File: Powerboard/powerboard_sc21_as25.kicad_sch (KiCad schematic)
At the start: 43 parts

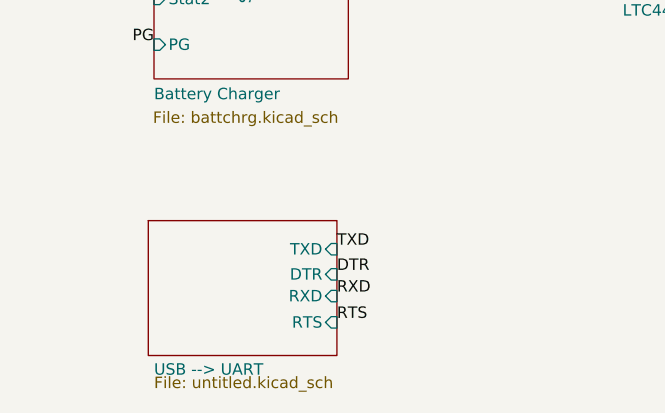
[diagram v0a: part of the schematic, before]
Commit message: added vbus to 3.3v converter
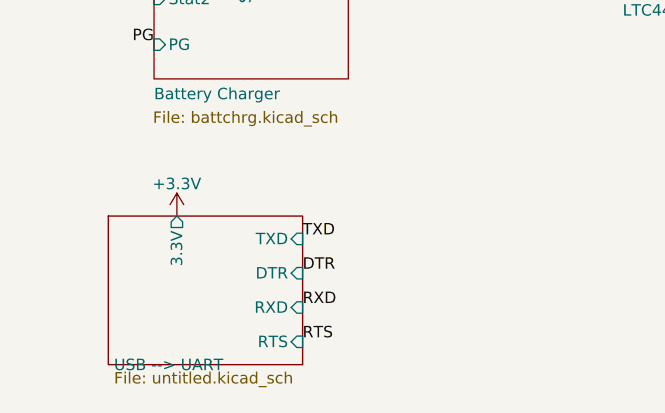
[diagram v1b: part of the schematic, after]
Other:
- sheet USB --> UART ports: added 3.3V; removed none
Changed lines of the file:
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@@
     (effects (font (size 1.27 1.27)) (justify right bottom))
   )
-  (label "DTR" (at 67.31 174.117 0)
+  (label "DTR" (at 63.5 173.99 0)
     (effects (font (size 1.27 1.27)) (justify left bottom))
   )
@@
     (effects (font (size 1.27 1.27)) (justify left bottom))
   )
-  (label "TXD" (at 67.31 171.323 0)
+  (label "TXD" (at 63.5 170.18 0)
     (effects (font (size 1.27 1.27)) (justify left bottom))
   )
@@
     (effects (font (size 1.27 1.27)) (justify left bottom))
   )
-  (label "RXD" (at 67.31 176.53 0)
+  (label "RXD" (at 63.5 177.8 0)
     (effects (font (size 1.27 1.27)) (justify left bottom))
   )
@@
     (effects (font (size 1.27 1.27)) (justify left bottom))
   )
-  (label "RTS" (at 67.31 179.451 0)
+  (label "RTS" (at 63.5 181.61 0)
     (effects (font (size 1.27 1.27)) (justify left bottom))
   )
@@
     (pin "1")
   )
+  (symbol (lib_id "power:+3.3V") (at 49.53 167.64 0) (unit 1)
+    (in_bom yes) (on_board yes) (fields_autoplaced)
+    (property "Reference" "#PWR?" (id 0) (at 49.53 171.45 0)
+      (effects (font (size 1.27 1.27)) hide)
+    )
+    (property "Value" "+3.3V" (id 1) (at 49.53 164.0642 0))
+    (property "Footprint" "" (id 2) (at 49.53 167.64 0)
+      (effects (font (size 1.27 1.27)) hide)
+    )
+    (property "Datasheet" "" (id 3) (at 49.53 167.64 0)
+      (effects (font (size 1.27 1.27)) hide)
+    )
+    (pin "1")
+  )
   (symbol (lib_id "power:GND") (at 34.29 34.29 0) (unit 1)
     (in_bom yes) (on_board yes)
@@
     )
   )
-  (sheet (at 46.355 168.148) (size 20.955 14.986)
+  (sheet (at 41.91 167.64) (size 21.59 16.51)
     (stroke (width 0.1524) (type solid) (color 0 0 0 0))
     (fill (color 0 0 0 0.0000))
-    (property "Sheet name" "USB --> UART" (id 0) (at 46.99 185.42 0)
+    (property "Sheet name" "USB --> UART" (id 0) (at 42.545 184.912 0)
       (effects (font (size 1.27 1.27)) (justify left bottom))
     )
-    (property "Sheet file" "untitled.kicad_sch" (id 1) (at 46.99 185.42 0)
+    (property "Sheet file" "untitled.kicad_sch" (id 1) (at 42.545 184.912 0)
       (effects (font (size 1.27 1.27)) (justify left top))
     )
-    (pin "RXD" input (at 67.31 176.53 0)
+    (pin "DTR" input (at 63.5 173.99 0)
       (effects (font (size 1.27 1.27)) (justify right))
     )
-    (pin "DTR" input (at 67.31 174.117 0)
+    (pin "RXD" input (at 63.5 177.8 0)
       (effects (font (size 1.27 1.27)) (justify right))
     )
-    (pin "TXD" input (at 67.31 171.323 0)
+    (pin "TXD" input (at 63.5 170.18 0)
       (effects (font (size 1.27 1.27)) (justify right))
     )
-    (pin "RTS" input (at 67.31 179.451 0)
+    (pin "RTS" input (at 63.5 181.61 0)
+      (effects (font (size 1.27 1.27)) (justify right))
+    )
+    (pin "3.3V" output (at 49.53 167.64 90)
       (effects (font (size 1.27 1.27)) (justify right))
     )
@@
       (reference "#PWR?") (unit 1) (value "GND") (footprint "")
     )
+    (path "/b1853ee1-af2e-49ab-93e4-e29b2d9f793d/01b8be9d-07b4-4ed5-be0d-c2f1fdf5d66a"
+      (reference "#PWR?") (unit 1) (value "GND") (footprint "")
+    )
+    (path "/b1853ee1-af2e-49ab-93e4-e29b2d9f793d/0b35d416-2ef3-43da-b21e-3b5705733789"
+      (reference "#PWR?") (unit 1) (value "GND") (footprint "")
+    )
     (path "/1669a8b1-50be-401b-a425-d2de253f88c4"
       (reference "#PWR?") (unit 1) (value "GND") (footprint "")
@@
       (reference "#PWR?") (unit 1) (value "GND") (footprint "")
     )
+    (path "/b1853ee1-af2e-49ab-93e4-e29b2d9f793d/3e7fe04a-5983-45ca-b62b-77d9b2d44905"
+      (reference "#PWR?") (unit 1) (value "VBUS") (footprint "")
+    )
+    (path "/b1853ee1-af2e-49ab-93e4-e29b2d9f793d/53c2082f-14d4-4f8b-b15e-479d0706e172"
+      (reference "#PWR?") (unit 1) (value "GND") (footprint "")
+    )
     (path "/b1853ee1-af2e-49ab-93e4-e29b2d9f793d/5b143561-1a97-4458-adc9-ad22ebe9d9fc"
       (reference "#PWR?") (unit 1) (value "GND") (footprint "")
@@
       (reference "#PWR?") (unit 1) (value "+3.3V") (footprint "")
     )
+    (path "/7cdd1385-4bcf-4b79-addf-8e4216a2d506"
+      (reference "#PWR?") (unit 1) (value "+3.3V") (footprint "")
+    )
+    (path "/b1853ee1-af2e-49ab-93e4-e29b2d9f793d/7d0aa032-9b1f-469d-85cd-a28c4fe41bd4"
+      (reference "#PWR?") (unit 1) (value "GND") (footprint "")
+    )
     (path "/00000000-0000-0000-0000-000061beb629/7d5bd6a8-4feb-43d7-80fd-001ff51c8cd3"
       (reference "#PWR?") (unit 1) (value "GND") (footprint "")
@@
       (reference "#PWR?") (unit 1) (value "GND") (footprint "")
     )
+    (path "/b1853ee1-af2e-49ab-93e4-e29b2d9f793d/a2635da5-8463-46db-9199-0a173306f41b"
+      (reference "#PWR?") (unit 1) (value "GND") (footprint "")
+    )
     (path "/a313493b-a610-47cf-bd19-ffd9120f658d"
       (reference "#PWR?") (unit 1) (value "+3.3V") (footprint "")
     )
+    (path "/b1853ee1-af2e-49ab-93e4-e29b2d9f793d/a4e693f1-e8be-4638-b20a-f43f39a9ed46"
+      (reference "#PWR?") (unit 1) (value "GND") (footprint "")
+    )
+    (path "/b1853ee1-af2e-49ab-93e4-e29b2d9f793d/b36e399c-fd07-48dc-9ff5-2204b47fbf43"
+      (reference "#PWR?") (unit 1) (value "GND") (footprint "")
+    )
     (path "/b1853ee1-af2e-49ab-93e4-e29b2d9f793d/b3eace1a-8e3b-4ab2-9e5a-cfb096644465"
       (reference "#PWR?") (unit 1) (value "+3.3V") (footprint "")
     )
+    (path "/b1853ee1-af2e-49ab-93e4-e29b2d9f793d/ba910aa5-1c14-49e2-8e02-8063979f6496"
+      (reference "#PWR?") (unit 1) (value "GND") (footprint "")
+    )
     (path "/c564c3d3-cbea-454d-bfac-67a8a729bdf8"
       (reference "#PWR?") (unit 1) (value "GND") (footprint "")
@@
       (reference "C?") (unit 1) (value "CP") (footprint "")
     )
+    (path "/b1853ee1-af2e-49ab-93e4-e29b2d9f793d/02e53112-42dc-4e92-9413-ebf4a1fcdc4a"
+      (reference "C?") (unit 1) (value "10uF") (footprint "Capacitor_SMD:C_0603_1608Metric")
+    )
+    (path "/b1853ee1-af2e-49ab-93e4-e29b2d9f793d/19b6fdb7-c2da-4e40-b2bb-be0a937611f0"
+      (reference "C?") (unit 1) (value "4.7uF") (footprint "Capacitor_SMD:C_0603_1608Metric")
+    )
+    (path "/b1853ee1-af2e-49ab-93e4-e29b2d9f793d/1fd2c422-69ae-40c0-b3b2-cb505077339f"
+      (reference "C?") (unit 1) (value "0.1uF") (footprint "Capacitor_SMD:C_0603_1608Metric")
+    )
     (path "/b1853ee1-af2e-49ab-93e4-e29b2d9f793d/23d7c986-ca1f-4e54-a551-aae82e6382e3"
       (reference "C?") (unit 1) (value "1.0muF") (footprint "")
@@
       (reference "C?") (unit 1) (value "1μF") (footprint "")
     )
+    (path "/b1853ee1-af2e-49ab-93e4-e29b2d9f793d/3bf9d9e3-3041-4ea1-ad6f-34bc1dc2c61a"
+      (reference "C?") (unit 1) (value "1uF") (footprint "Capacitor_SMD:C_0603_1608Metric")
+    )
     (path "/b1853ee1-af2e-49ab-93e4-e29b2d9f793d/400c7a12-6a3b-4007-bebb-25fa9d8ef61f"
       (reference "C?") (unit 1) (value "0.1muF") (footprint "")
@@
       (reference "C?") (unit 1) (value "4.7muF") (footprint "")
     )
+    (path "/b1853ee1-af2e-49ab-93e4-e29b2d9f793d/900cbe97-baf8-4c02-a824-562c02dac994"
+      (reference "C?") (unit 1) (value "10uF") (footprint "Capacitor_SMD:C_0603_1608Metric")
+    )
     (path "/96d17e45-ecc3-4647-9d46-ac8a08d006bc"
       (reference "C?") (unit 1) (value "1.5pF") (footprint "")
@@
       (reference "R?") (unit 1) (value "470Ω") (footprint "")
     )
+    (path "/b1853ee1-af2e-49ab-93e4-e29b2d9f793d/08599c5d-18df-4076-8d95-9afe2b0b7202"
+      (reference "R?") (unit 1) (value "100k") (footprint "Resistor_SMD:R_0603_1608Metric")
+    )
+    (path "/b1853ee1-af2e-49ab-93e4-e29b2d9f793d/1f07eb91-ef46-4237-a9f5-5823737e0d44"
+      (reference "R?") (unit 1) (value "47k") (footprint "Resistor_SMD:R_0603_1608Metric")
+    )
     (path "/b1853ee1-af2e-49ab-93e4-e29b2d9f793d/3fdc1205-170d-4bad-a583-c2274b810ac0"
       (reference "R?") (unit 1) (value "47k") (footprint "")
@@
       (reference "R?") (unit 1) (value "10kΩ") (footprint "")
     )
+    (path "/b1853ee1-af2e-49ab-93e4-e29b2d9f793d/a6bf9111-8852-4077-bff6-579c92450f65"
+      (reference "R?") (unit 1) (value "147k") (footprint "Resistor_SMD:R_0603_1608Metric")
+    )
     (path "/b1853ee1-af2e-49ab-93e4-e29b2d9f793d/a97adbbf-7a4b-4c74-8340-d0fb219e42dc"
       (reference "R?") (unit 1) (value "5.1k") (footprint "")
@@
       (reference "U?") (unit 1) (value "LTC4412xS6") (footprint "Package_TO_SOT_SMD:TSOT-23-6")
     )
-  )
+    (path "/b1853ee1-af2e-49ab-93e4-e29b2d9f793d/1444d49f-1253-44c6-b265-5d56e5057df7"
+      (reference "U?") (unit 1) (value "RT9025-25GSP") (footprint "Package_SO:SOP-8_3.9x4.9mm_P1.27mm")
+    )
+    (path "/b1853ee1-af2e-49ab-93e4-e29b2d9f793d/8f776380-fcbf-4da6-96c0-055517925d40"
+      (reference "U?") (unit 1) (value "LTC4411") (footprint "Package_TO_SOT_SMD:SOT-23-5")
+    )
+  )

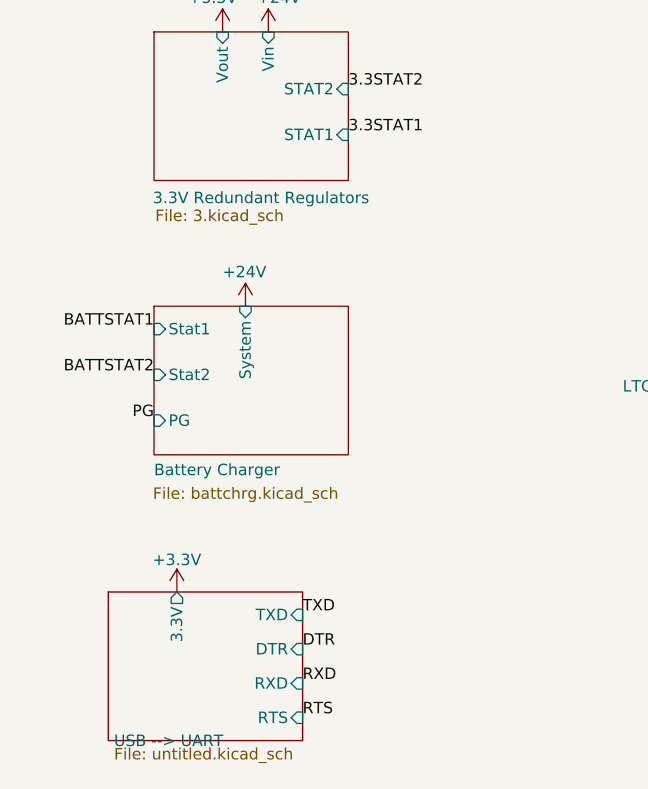
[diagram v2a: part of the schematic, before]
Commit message: Added thermistor resistor for specific thermistor
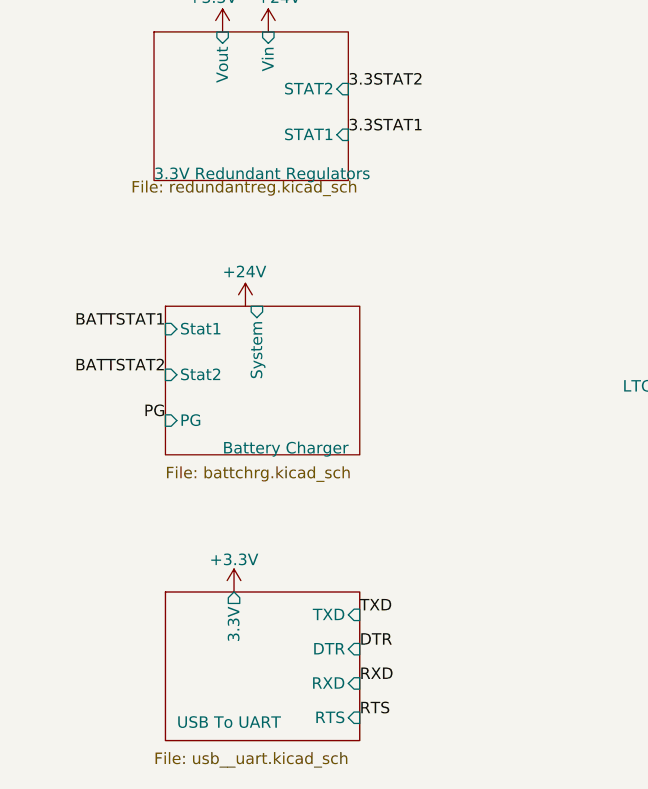
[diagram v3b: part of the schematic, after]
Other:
- sheet USB --> UART renamed USB To UART
- sheet 3.3V Redundant Regulators: file 3.kicad_sch -> redundantreg.kicad_sch
- sheet USB To UART: file untitled.kicad_sch -> usb__uart.kicad_sch
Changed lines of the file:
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@@
     (effects (font (size 1.27 1.27)) (justify left bottom))
   )
-  (label "BATTSTAT1" (at 46.99 138.43 180)
+  (label "BATTSTAT1" (at 48.26 138.43 180)
     (effects (font (size 1.27 1.27)) (justify right bottom))
   )
@@
     (effects (font (size 1.27 1.27)) (justify right bottom))
   )
-  (label "DTR" (at 63.5 173.99 0)
+  (label "DTR" (at 69.85 173.99 0)
     (effects (font (size 1.27 1.27)) (justify left bottom))
   )
@@
     (effects (font (size 1.27 1.27)) (justify left bottom))
   )
-  (label "TXD" (at 63.5 170.18 0)
+  (label "TXD" (at 69.85 170.18 0)
     (effects (font (size 1.27 1.27)) (justify left bottom))
   )
@@
     (effects (font (size 1.27 1.27)) (justify left bottom))
   )
-  (label "RXD" (at 63.5 177.8 0)
+  (label "RXD" (at 69.85 177.8 0)
     (effects (font (size 1.27 1.27)) (justify left bottom))
   )
@@
     (effects (font (size 1.27 1.27)) (justify left bottom))
   )
-  (label "RTS" (at 63.5 181.61 0)
+  (label "RTS" (at 69.85 181.61 0)
     (effects (font (size 1.27 1.27)) (justify left bottom))
   )
@@
     (effects (font (size 1.27 1.27)) (justify right bottom))
   )
-  (label "BATTSTAT2" (at 46.99 143.51 180)
+  (label "BATTSTAT2" (at 48.26 143.51 180)
     (effects (font (size 1.27 1.27)) (justify right bottom))
   )
@@
     (effects (font (size 1.27 1.27)) (justify left bottom))
   )
-  (label "PG" (at 46.99 148.59 180)
+  (label "PG" (at 48.26 148.59 180)
     (effects (font (size 1.27 1.27)) (justify right bottom))
   )
@@
     (pin "1")
   )
-  (symbol (lib_id "power:+3.3V") (at 49.53 167.64 0) (unit 1)
+  (symbol (lib_id "power:+3.3V") (at 55.88 167.64 0) (unit 1)
     (in_bom yes) (on_board yes) (fields_autoplaced)
-    (property "Reference" "#PWR?" (id 0) (at 49.53 171.45 0)
-      (effects (font (size 1.27 1.27)) hide)
-    )
-    (property "Value" "+3.3V" (id 1) (at 49.53 164.0642 0))
-    (property "Footprint" "" (id 2) (at 49.53 167.64 0)
-      (effects (font (size 1.27 1.27)) hide)
-    )
-    (property "Datasheet" "" (id 3) (at 49.53 167.64 0)
+    (property "Reference" "#PWR?" (id 0) (at 55.88 171.45 0)
+      (effects (font (size 1.27 1.27)) hide)
+    )
+    (property "Value" "+3.3V" (id 1) (at 55.88 164.0642 0))
+    (property "Footprint" "" (id 2) (at 55.88 167.64 0)
+      (effects (font (size 1.27 1.27)) hide)
+    )
+    (property "Datasheet" "" (id 3) (at 55.88 167.64 0)
       (effects (font (size 1.27 1.27)) hide)
     )
@@
     (pin "2")
   )
-  (sheet (at 46.99 135.89) (size 21.59 16.51)
+  (sheet (at 48.26 135.89) (size 21.59 16.51)
     (stroke (width 0) (type solid) (color 0 0 0 0))
     (fill (color 0 0 0 0.0000))
-    (property "Sheet name" "Battery Charger" (id 0) (at 46.99 154.813 0)
+    (property "Sheet name" "Battery Charger" (id 0) (at 54.61 152.4 0)
       (effects (font (size 1.27 1.27)) (justify left bottom))
     )
-    (property "Sheet file" "battchrg.kicad_sch" (id 1) (at 46.863 155.956 0)
+    (property "Sheet file" "battchrg.kicad_sch" (id 1) (at 48.26 153.67 0)
       (effects (font (size 1.27 1.27)) (justify left top))
     )
-    (pin "System" input (at 57.15 135.89 90)
+    (pin "System" input (at 58.42 135.89 90)
       (effects (font (size 1.27 1.27)) (justify right))
     )
-    (pin "Stat1" input (at 46.99 138.43 180)
-      (effects (font (size 1.27 1.27)) (justify left))
-    )
-    (pin "Stat2" input (at 46.99 143.51 180)
-      (effects (font (size 1.27 1.27)) (justify left))
-    )
-    (pin "PG" input (at 46.99 148.59 180)
+    (pin "Stat1" input (at 48.26 138.43 180)
+      (effects (font (size 1.27 1.27)) (justify left))
+    )
+    (pin "Stat2" input (at 48.26 143.51 180)
+      (effects (font (size 1.27 1.27)) (justify left))
+    )
+    (pin "PG" input (at 48.26 148.59 180)
       (effects (font (size 1.27 1.27)) (justify left))
     )
@@
     (stroke (width 0) (type solid) (color 0 0 0 0))
     (fill (color 0 0 0 0.0000))
-    (property "Sheet name" "3.3V Redundant Regulators" (id 0) (at 46.863 124.587 0)
+    (property "Sheet name" "3.3V Redundant Regulators" (id 0) (at 46.99 121.92 0)
       (effects (font (size 1.27 1.27)) (justify left bottom))
     )
-    (property "Sheet file" "3.kicad_sch" (id 1) (at 47.117 125.095 0)
+    (property "Sheet file" "redundantreg.kicad_sch" (id 1) (at 44.45 121.92 0)
       (effects (font (size 1.27 1.27)) (justify left top))
     )
@@
     )
   )
-  (sheet (at 41.91 167.64) (size 21.59 16.51)
+  (sheet (at 48.26 167.64) (size 21.59 16.51)
     (stroke (width 0.1524) (type solid) (color 0 0 0 0))
     (fill (color 0 0 0 0.0000))
-    (property "Sheet name" "USB --> UART" (id 0) (at 42.545 184.912 0)
+    (property "Sheet name" "USB To UART" (id 0) (at 49.53 182.88 0)
       (effects (font (size 1.27 1.27)) (justify left bottom))
     )
-    (property "Sheet file" "untitled.kicad_sch" (id 1) (at 42.545 184.912 0)
+    (property "Sheet file" "usb__uart.kicad_sch" (id 1) (at 46.99 185.42 0)
       (effects (font (size 1.27 1.27)) (justify left top))
     )
-    (pin "DTR" input (at 63.5 173.99 0)
+    (pin "DTR" input (at 69.85 173.99 0)
       (effects (font (size 1.27 1.27)) (justify right))
     )
-    (pin "RXD" input (at 63.5 177.8 0)
+    (pin "RXD" input (at 69.85 177.8 0)
       (effects (font (size 1.27 1.27)) (justify right))
     )
-    (pin "TXD" input (at 63.5 170.18 0)
+    (pin "TXD" input (at 69.85 170.18 0)
       (effects (font (size 1.27 1.27)) (justify right))
     )
-    (pin "RTS" input (at 63.5 181.61 0)
+    (pin "RTS" input (at 69.85 181.61 0)
       (effects (font (size 1.27 1.27)) (justify right))
     )
-    (pin "3.3V" output (at 49.53 167.64 90)
+    (pin "3.3V" output (at 55.88 167.64 90)
       (effects (font (size 1.27 1.27)) (justify right))
     )
@@
     )
     (path "/00000000-0000-0000-0000-000061beb629/00000000-0000-0000-0000-000061c1bdf7"
-      (reference "J1") (unit 1) (value "Thermistor Connection") (footprint "")
+      (reference "J1") (unit 1) (value "Thermistor Connection 103AT NTC") (footprint "")
     )
     (path "/00000000-0000-0000-0000-0000620cf89f"

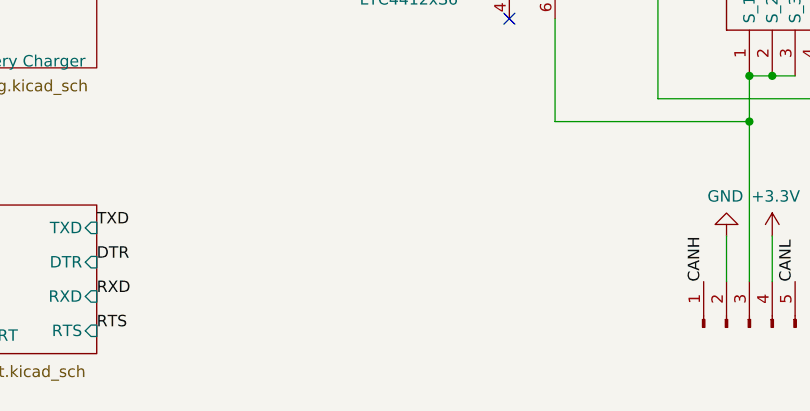
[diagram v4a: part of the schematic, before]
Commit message: removed battery monitor
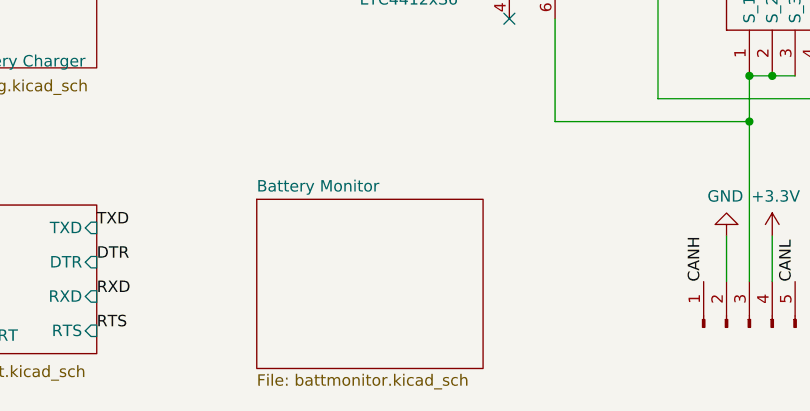
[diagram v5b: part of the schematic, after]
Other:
- added sheet Battery Monitor (battmonitor.kicad_sch)
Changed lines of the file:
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@@
+    )
+  )
+  (sheet (at 87.63 167.005) (size 25.146 18.796) (fields_autoplaced)
+    (stroke (width 0.1524) (type solid) (color 0 0 0 0))
+    (fill (color 0 0 0 0.0000))
+    (property "Sheet name" "Battery Monitor" (id 0) (at 87.63 166.2934 0)
+      (effects (font (size 1.27 1.27)) (justify left bottom))
+    )
+    (property "Sheet file" "battmonitor.kicad_sch" (id 1) (at 87.63 186.3856 0)
+      (effects (font (size 1.27 1.27)) (justify left top))
     )
   )
@@
     (path "/00000000-0000-0000-0000-000061f04c1a" (page "3"))
     (path "/b1853ee1-af2e-49ab-93e4-e29b2d9f793d" (page "4"))
+    (path "/33e9abb9-e634-4336-bd82-f9f25ebb0731" (page "5"))
   )
   (symbol_instances
@@
       (reference "IC?") (unit 1) (value "CP2102") (footprint "QFN50P500X500X100-29N-D")
     )
+    (path "/33e9abb9-e634-4336-bd82-f9f25ebb0731/c1d61362-65a2-49c7-92c4-42116f69f186"
+      (reference "IC?") (unit 1) (value "BQ34Z110PWR") (footprint "SOP65P640X120-14N")
+    )
     (path "/00000000-0000-0000-0000-000061beb629/00000000-0000-0000-0000-000061c1bdf7"
       (reference "J1") (unit 1) (value "Thermistor Connection 103AT NTC") (footprint "")
@@
       (reference "R3") (unit 1) (value "100kΩ") (footprint "")
     )
-    (path "/00000000-0000-0000-0000-000061beb629/00000000-0000-0000-0000-000061c1be29"
-      (reference "R4") (unit 1) (value "150kΩ") (footprint "")
-    )
     (path "/00000000-0000-0000-0000-000061beb629/00000000-0000-0000-0000-000061c1be1d"
       (reference "R5") (unit 1) (value "100kΩ") (footprint "")
     )
-    (path "/00000000-0000-0000-0000-000061beb629/00000000-0000-0000-0000-000061c1be2f"
-      (reference "R6") (unit 1) (value "13kΩ") (footprint "")
-    )
     (path "/00000000-0000-0000-0000-000061beb629/00000000-0000-0000-0000-000061c1be11"
       (reference "R7") (unit 1) (value "100kΩ") (footprint "")
     )
-    (path "/00000000-0000-0000-0000-000061beb629/00000000-0000-0000-0000-000061c1be23"
-      (reference "R8") (unit 1) (value "32kΩ") (footprint "")
-    )
     (path "/00000000-0000-0000-0000-000061beb629/00000000-0000-0000-0000-000061c1bdd5"
       (reference "R9") (unit 1) (value "9.31kΩ") (footprint "")
@@
       (reference "RAC") (unit 1) (value "10mΩ") (footprint "")
     )
+    (path "/00000000-0000-0000-0000-000061beb629/00000000-0000-0000-0000-000061c1be29"
+      (reference "RAdp") (unit 1) (value "150kΩ") (footprint "")
+    )
+    (path "/00000000-0000-0000-0000-000061beb629/00000000-0000-0000-0000-000061c1be23"
+      (reference "RFast") (unit 1) (value "32kΩ") (footprint "")
+    )
+    (path "/00000000-0000-0000-0000-000061beb629/00000000-0000-0000-0000-000061c1be2f"
+      (reference "RPre") (unit 1) (value "13kΩ") (footprint "")
+    )
     (path "/00000000-0000-0000-0000-000061beb629/00000000-0000-0000-0000-000061c2a94c"
